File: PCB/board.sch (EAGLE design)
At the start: 9 parts, among them J1 PROG-HEADER_2X3_SHROUDED, J10 PROG-HEADER_2X5_1.27MM-SHROUD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, J2 PROG-HEADER_2X5_2.00MM-SHROUD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, J3 PROG-HEADER_2X5_SHROUDED, J4 PROG-HEADER_2X10_2.54MM-END-L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, J6 PROG-HEADER_2X10_SHROUDED, J8 CONN-1X4, J9 CONN-1X6

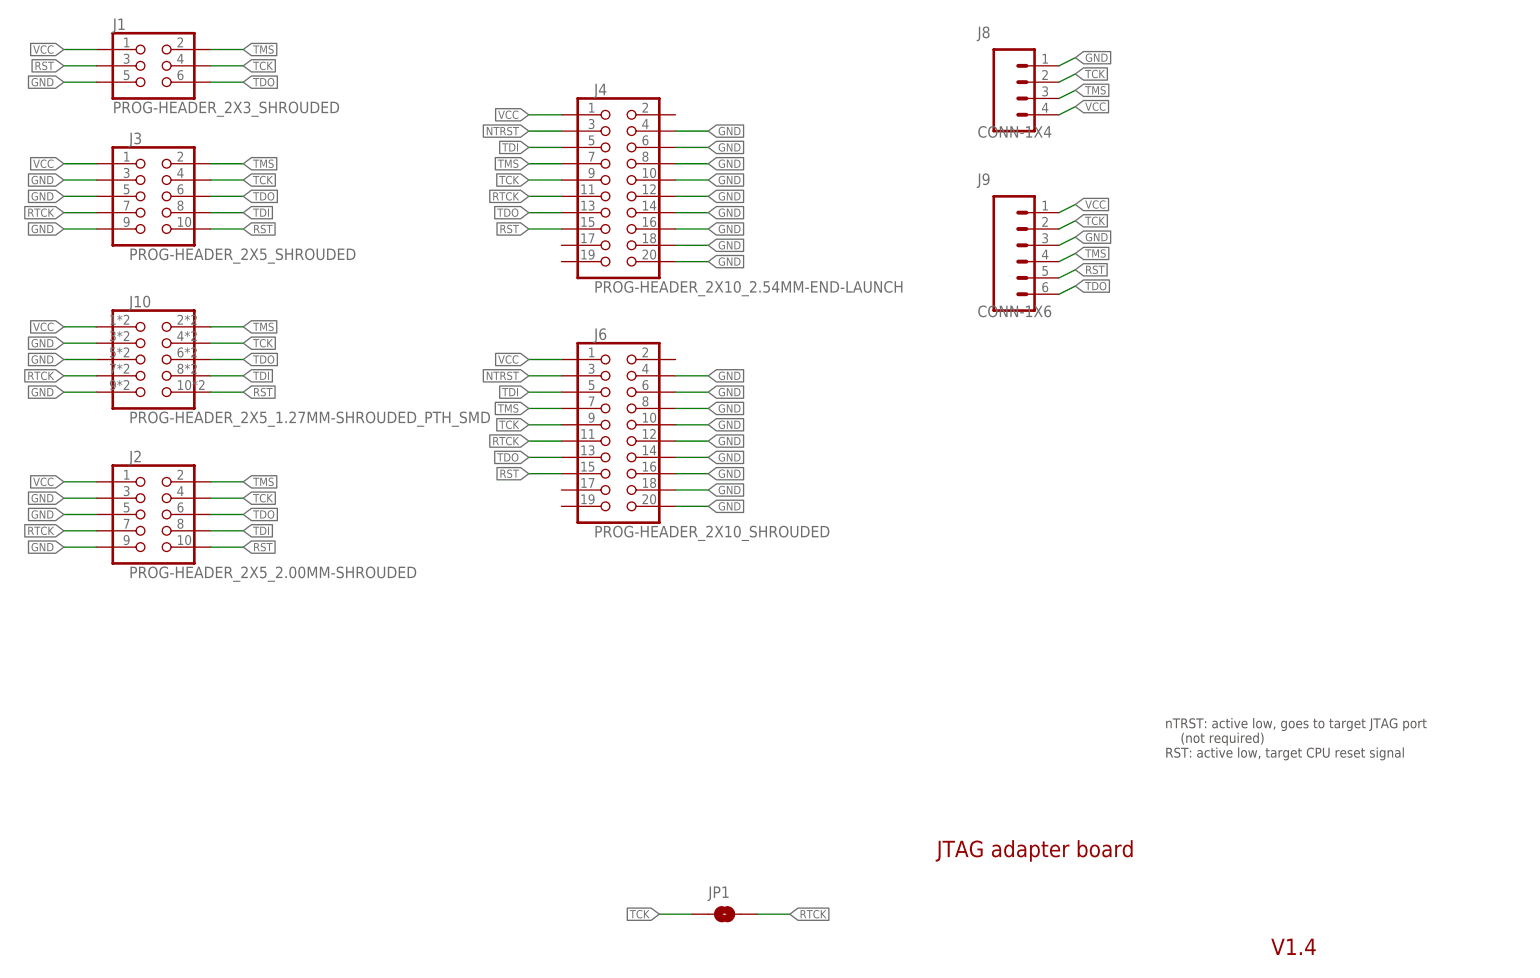
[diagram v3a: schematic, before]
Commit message: V1.5
 - changed RST to TDI for 3*2 pin connector
 - optimized routing
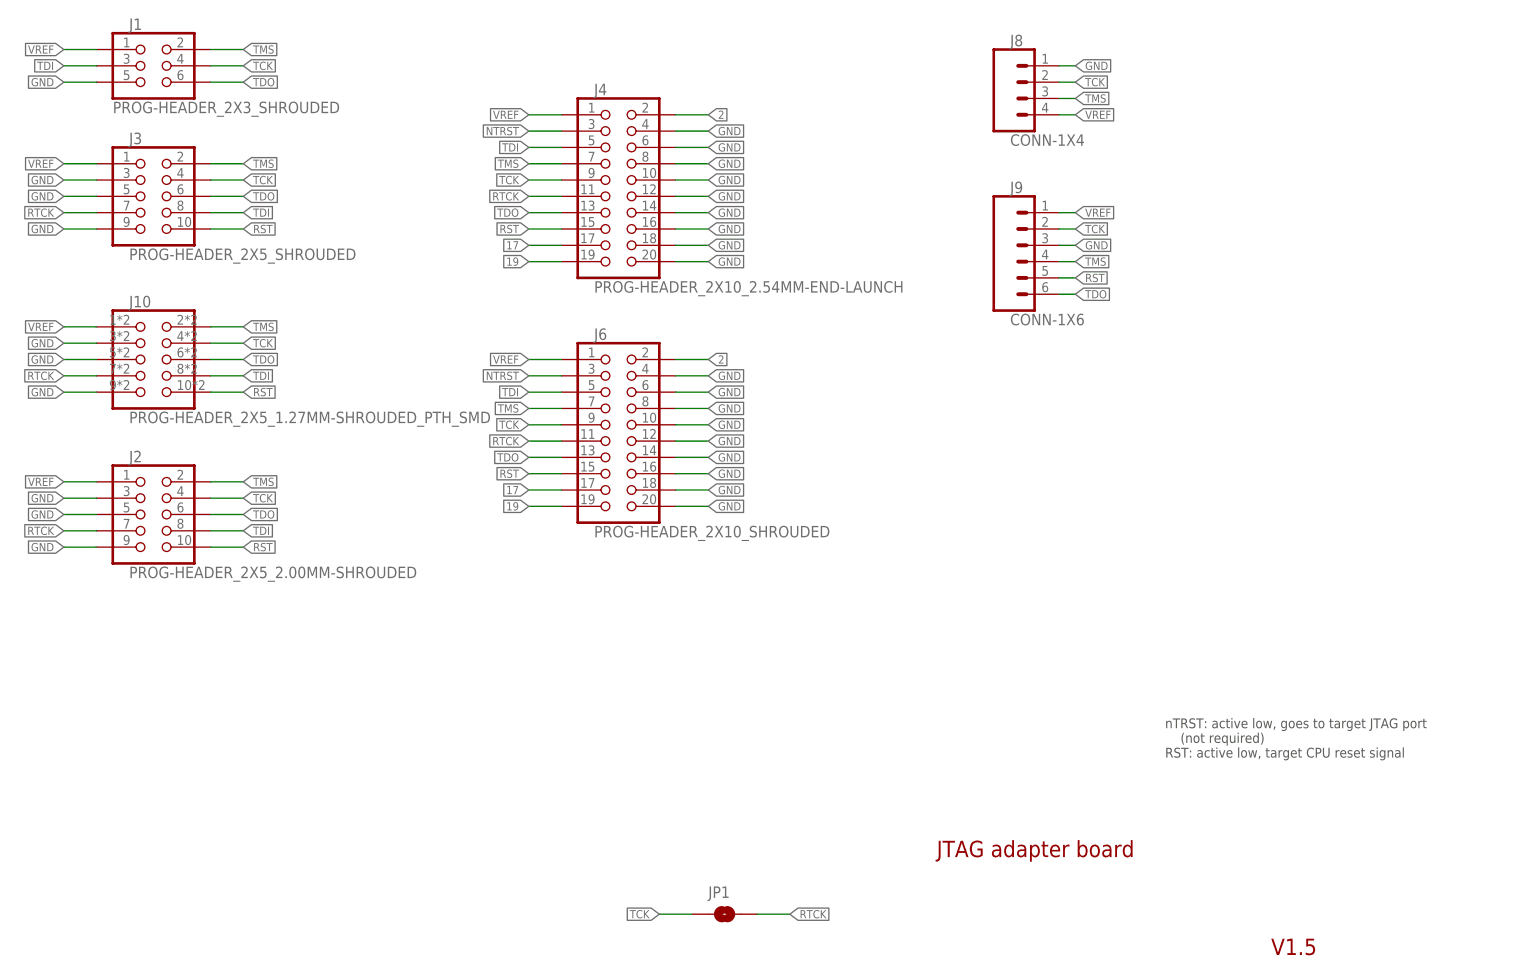
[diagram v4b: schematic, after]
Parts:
- JP1: device SparkFun-Jumpers:JUMPER-SMT_2_NO_SILK -> angrypig7-Jumpers:JUMPER-SMT_2_NO_SILK
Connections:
- net VCC renamed VREF
- new net 17: J4.17, J6.17
- new net 19: J4.19, J6.19
- new net 2: J4.2, J6.2
- net RST: no longer J1.3
- net TDI: now also J1.3
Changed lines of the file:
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@@
 <?xml version="1.0" encoding="utf-8"?>
 <!DOCTYPE eagle SYSTEM "eagle.dtd">
-<eagle version="9.6.1">
+<eagle version="9.6.2">
 <drawing>
 <settings>
@@
 <attributes>
 <attribute name="CNAME" value="JTAG adapter board"/>
-<attribute name="CREVISION" value="V1.4"/>
+<attribute name="CREVISION" value="V1.5"/>
 </attributes>
 <variantdefs>
@@
 <part name="J8" library="angrypig7-Connectors-Programming" deviceset="CONN-1X4" device=""/>
 <part name="J9" library="angrypig7-Connectors-Programming" deviceset="CONN-1X6" device=""/>
-<part name="JP1" library="SparkFun-Jumpers" deviceset="JUMPER-SMT_2_NO" device="_SILK" package3d_urn="urn:adsk.eagle:package:39279/1" value="TCK-RTCK"/>
+<part name="JP1" library="angrypig7-Jumpers" deviceset="JUMPER-SMT_2_NO" device="_SILK" package3d_urn="urn:adsk.eagle:package:39279/1" value="TCK-RTCK"/>
 <part name="J10" library="angrypig7-Connectors-Programming" deviceset="PROG-HEADER_2X5" device="_1.27MM-SHROUDED_PTH_SMD" value="PROG-HEADER_2X5_1.27MM-SHROUDED_PTH_SMD"/>
 <part name="J2" library="angrypig7-Connectors-Programming" deviceset="PROG-HEADER_2X5" device="_2.00MM-SHROUDED"/>
@@
 </instance>
 <instance part="J1" gate="G$1" x="63.5" y="143.51" smashed="yes">
-<attribute name="NAME" x="57.15" y="149.098" size="1.778" layer="95" font="vector"/>
+<attribute name="NAME" x="59.69" y="149.098" size="1.778" layer="95" font="vector"/>
 <attribute name="VALUE" x="57.15" y="136.144" size="1.778" layer="96" font="vector"/>
 </instance>
@@
 </instance>
 <instance part="J8" gate="G$1" x="196.85" y="139.7" smashed="yes">
-<attribute name="VALUE" x="191.77" y="132.334" size="1.778" layer="96" font="vector"/>
-<attribute name="NAME" x="191.77" y="147.828" size="1.778" layer="95" font="vector"/>
+<attribute name="VALUE" x="196.85" y="131.064" size="1.778" layer="96" font="vector"/>
+<attribute name="NAME" x="196.85" y="146.558" size="1.778" layer="95" font="vector"/>
 </instance>
 <instance part="J9" gate="G$1" x="196.85" y="114.3" smashed="yes">
-<attribute name="VALUE" x="191.77" y="104.394" size="1.778" layer="96" font="vector"/>
-<attribute name="NAME" x="191.77" y="124.968" size="1.778" layer="95" font="vector"/>
+<attribute name="VALUE" x="196.85" y="103.124" size="1.778" layer="96" font="vector"/>
+<attribute name="NAME" x="196.85" y="123.698" size="1.778" layer="95" font="vector"/>
 </instance>
 <instance part="JP1" gate="G$1" x="152.4" y="11.43" smashed="yes">
@@
 </busses>
 <nets>
-<net name="VCC" class="0">
+<net name="VREF" class="0">
 <segment>
 <wire x1="54.61" y1="128.27" x2="49.53" y2="128.27" width="0.1524" layer="91"/>
@@
 </segment>
 <segment>
-<wire x1="204.47" y1="135.89" x2="207.01" y2="137.16" width="0.1524" layer="91"/>
-<label x="207.01" y="137.16" size="1.27" layer="95" xref="yes"/>
+<wire x1="204.47" y1="135.89" x2="207.01" y2="135.89" width="0.1524" layer="91"/>
+<label x="207.01" y="135.89" size="1.27" layer="95" xref="yes"/>
 <pinref part="J8" gate="G$1" pin="4"/>
 </segment>
 <segment>
-<label x="207.01" y="121.92" size="1.27" layer="95" xref="yes"/>
+<label x="207.01" y="120.65" size="1.27" layer="95" xref="yes"/>
 <pinref part="J9" gate="G$1" pin="1"/>
-<wire x1="207.01" y1="121.92" x2="204.47" y2="120.65" width="0.1524" layer="91"/>
+<wire x1="207.01" y1="120.65" x2="204.47" y2="120.65" width="0.1524" layer="91"/>
 </segment>
 <segment>
@@
 </segment>
 <segment>
-<wire x1="204.47" y1="138.43" x2="207.01" y2="139.7" width="0.1524" layer="91"/>
-<label x="207.01" y="139.7" size="1.27" layer="95" xref="yes"/>
+<wire x1="204.47" y1="138.43" x2="207.01" y2="138.43" width="0.1524" layer="91"/>
+<label x="207.01" y="138.43" size="1.27" layer="95" xref="yes"/>
 <pinref part="J8" gate="G$1" pin="3"/>
 </segment>
@@
 </segment>
 <segment>
-<label x="207.01" y="114.3" size="1.27" layer="95" xref="yes"/>
+<label x="207.01" y="113.03" size="1.27" layer="95" xref="yes"/>
 <pinref part="J9" gate="G$1" pin="4"/>
-<wire x1="204.47" y1="113.03" x2="207.01" y2="114.3" width="0.1524" layer="91"/>
+<wire x1="204.47" y1="113.03" x2="207.01" y2="113.03" width="0.1524" layer="91"/>
 </segment>
 </net>
@@
 </segment>
 <segment>
-<label x="207.01" y="109.22" size="1.27" layer="95" xref="yes"/>
+<label x="207.01" y="107.95" size="1.27" layer="95" xref="yes"/>
 <pinref part="J9" gate="G$1" pin="6"/>
-<wire x1="204.47" y1="107.95" x2="207.01" y2="109.22" width="0.1524" layer="91"/>
+<wire x1="204.47" y1="107.95" x2="207.01" y2="107.95" width="0.1524" layer="91"/>
 </segment>
 </net>
@@
 <pinref part="J4" gate="G$1" pin="5"/>
 </segment>
+<segment>
+<wire x1="54.61" y1="143.51" x2="49.53" y2="143.51" width="0.1524" layer="91"/>
+<label x="49.53" y="143.51" size="1.27" layer="95" rot="R180" xref="yes"/>
+<pinref part="J1" gate="G$1" pin="3"/>
+</segment>
 </net>
 <net name="RST" class="0">
@@
 </segment>
 <segment>
-<wire x1="54.61" y1="143.51" x2="49.53" y2="143.51" width="0.1524" layer="91"/>
-<label x="49.53" y="143.51" size="1.27" layer="95" rot="R180" xref="yes"/>
-<pinref part="J1" gate="G$1" pin="3"/>
-</segment>
-<segment>
 <wire x1="72.39" y1="92.71" x2="77.47" y2="92.71" width="0.1524" layer="91"/>
 <label x="77.47" y="92.71" size="1.27" layer="95" xref="yes"/>
@@
 </segment>
 <segment>
-<label x="207.01" y="111.76" size="1.27" layer="95" xref="yes"/>
+<label x="207.01" y="110.49" size="1.27" layer="95" xref="yes"/>
 <pinref part="J9" gate="G$1" pin="5"/>
-<wire x1="204.47" y1="110.49" x2="207.01" y2="111.76" width="0.1524" layer="91"/>
+<wire x1="204.47" y1="110.49" x2="207.01" y2="110.49" width="0.1524" layer="91"/>
 </segment>
 </net>
@@
 </segment>
 <segment>
-<wire x1="204.47" y1="143.51" x2="207.01" y2="144.78" width="0.1524" layer="91"/>
-<label x="207.01" y="144.78" size="1.27" layer="95" xref="yes"/>
+<wire x1="204.47" y1="143.51" x2="207.01" y2="143.51" width="0.1524" layer="91"/>
+<label x="207.01" y="143.51" size="1.27" layer="95" xref="yes"/>
 <pinref part="J8" gate="G$1" pin="1"/>
 </segment>
@@
 </segment>
 <segment>
-<label x="207.01" y="116.84" size="1.27" layer="95" xref="yes"/>
+<label x="207.01" y="115.57" size="1.27" layer="95" xref="yes"/>
 <pinref part="J9" gate="G$1" pin="3"/>
-<wire x1="207.01" y1="116.84" x2="204.47" y2="115.57" width="0.1524" layer="91"/>
+<wire x1="207.01" y1="115.57" x2="204.47" y2="115.57" width="0.1524" layer="91"/>
 </segment>
 <segment>
@@
 <net name="TCK" class="0">
 <segment>
-<wire x1="204.47" y1="140.97" x2="207.01" y2="142.24" width="0.1524" layer="91"/>
-<label x="207.01" y="142.24" size="1.27" layer="95" xref="yes"/>
+<wire x1="204.47" y1="140.97" x2="207.01" y2="140.97" width="0.1524" layer="91"/>
+<label x="207.01" y="140.97" size="1.27" layer="95" xref="yes"/>
 <pinref part="J8" gate="G$1" pin="2"/>
 </segment>
@@
 </segment>
 <segment>
-<label x="207.01" y="119.38" size="1.27" layer="95" xref="yes"/>
+<label x="207.01" y="118.11" size="1.27" layer="95" xref="yes"/>
 <pinref part="J9" gate="G$1" pin="2"/>
-<wire x1="204.47" y1="118.11" x2="207.01" y2="119.38" width="0.1524" layer="91"/>
+<wire x1="204.47" y1="118.11" x2="207.01" y2="118.11" width="0.1524" layer="91"/>
 </segment>
 </net>
@@
 </segment>
 </net>
+<net name="2" class="0">
+<segment>
+<pinref part="J4" gate="G$1" pin="2"/>
+<wire x1="144.78" y1="135.89" x2="149.86" y2="135.89" width="0.1524" layer="91"/>
+<label x="149.86" y="135.89" size="1.27" layer="95" xref="yes"/>
+</segment>
+<segment>
+<pinref part="J6" gate="G$1" pin="2"/>
+<wire x1="144.78" y1="97.79" x2="149.86" y2="97.79" width="0.1524" layer="91"/>
+<label x="149.86" y="97.79" size="1.27" layer="95" xref="yes"/>
+</segment>
+</net>
+<net name="17" class="0">
+<segment>
+<pinref part="J6" gate="G$1" pin="17"/>
+<wire x1="127" y1="77.47" x2="121.92" y2="77.47" width="0.1524" layer="91"/>
+<label x="121.92" y="77.47" size="1.27" layer="95" rot="R180" xref="yes"/>
+</segment>
+<segment>
+<pinref part="J4" gate="G$1" pin="17"/>
+<wire x1="127" y1="115.57" x2="121.92" y2="115.57" width="0.1524" layer="91"/>
+<label x="121.92" y="115.57" size="1.27" layer="95" rot="R180" xref="yes"/>
+</segment>
+</net>
+<net name="19" class="0">
+<segment>
+<pinref part="J6" gate="G$1" pin="19"/>
+<wire x1="127" y1="74.93" x2="121.92" y2="74.93" width="0.1524" layer="91"/>
+<label x="121.92" y="74.93" size="1.27" layer="95" rot="R180" xref="yes"/>
+</segment>
+<segment>
+<pinref part="J4" gate="G$1" pin="19"/>
+<wire x1="127" y1="113.03" x2="121.92" y2="113.03" width="0.1524" layer="91"/>
+<label x="121.92" y="113.03" size="1.27" layer="95" rot="R180" xref="yes"/>
+</segment>
+</net>
